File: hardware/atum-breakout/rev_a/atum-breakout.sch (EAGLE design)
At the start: 71 parts, among them J1 TC2030-CTX, J2 TC2030-CC2538-BL, J3 SCREW-TERMINAL_8_0.100, J4 SCREW-TERMINAL_7_0.100, J5 SCREW-TERMINAL_7_0.100, J6 SCREW-TERMINAL_8_0.100, J7 MICRO_USB_B_HIROSE_ZX62R-B-5P, J8 SCREW-TERMINAL_3_0.100, J9 SCREW-TERMINAL_3_0.100, U1 ATUM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

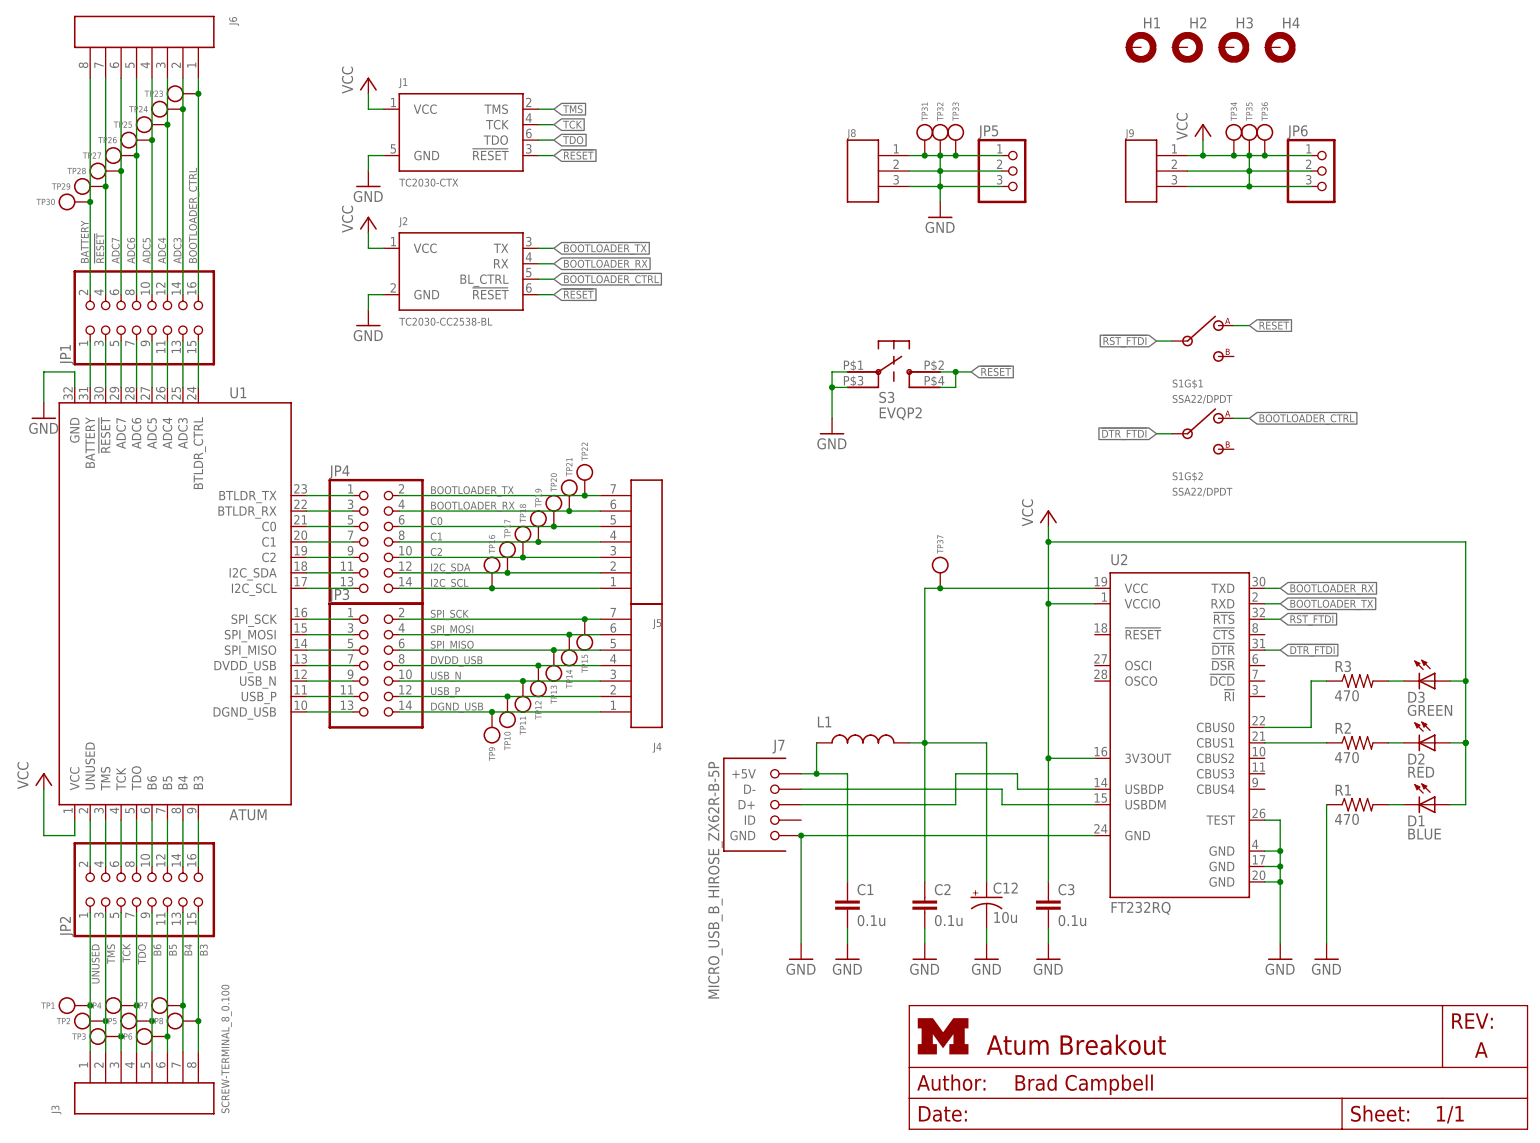
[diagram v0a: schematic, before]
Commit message: updated part labels
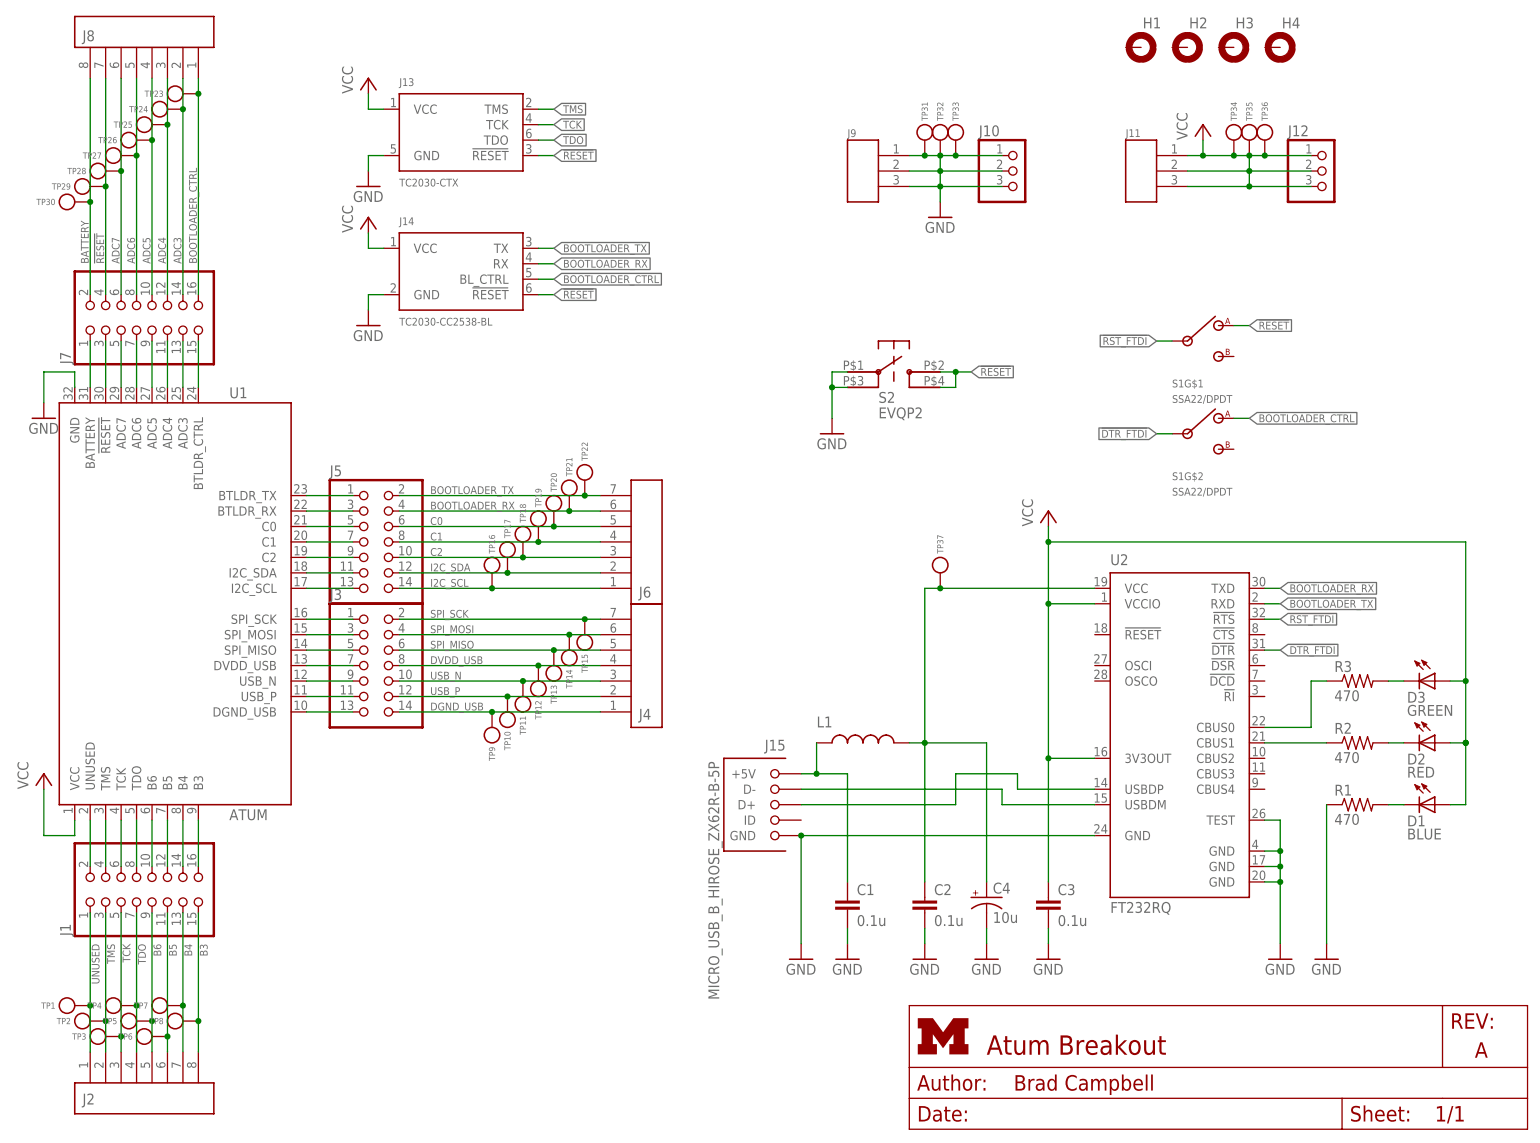
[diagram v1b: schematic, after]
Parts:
- removed JP1, JP2: (no value), pinhead:PINHD-2X8
- removed JP3, JP4: (no value), pinhead:PINHD-2X7
- added J11: SCREW-TERMINAL_3_0.100, headers:SCREW-TERMINAL_3_0.100
- added J13: TC2030-CTX, connector:TC2030-CTX
- added J14: TC2030-CC2538-BL, connector:TC2030-CC2538-BL
- added J15: MICRO_USB_B_HIROSE_ZX62R-B-5P, connector:MICRO_USB_B_HIROSE_ZX62R-B-5P
- J1: value TC2030-CTX -> (none); device connector:TC2030-CTX -> pinhead:PINHD-2X8
- J2: value TC2030-CC2538-BL -> SCREW-TERMINAL_8_0.100; device connector:TC2030-CC2538-BL -> headers:SCREW-TERMINAL_8_0.100
- J3: value SCREW-TERMINAL_8_0.100 -> (none); device headers:SCREW-TERMINAL_8_0.100 -> pinhead:PINHD-2X7
- J5: value SCREW-TERMINAL_7_0.100 -> (none); device headers:SCREW-TERMINAL_7_0.100 -> pinhead:PINHD-2X7
- J6: value SCREW-TERMINAL_8_0.100 -> SCREW-TERMINAL_7_0.100; device headers:SCREW-TERMINAL_8_0.100 -> headers:SCREW-TERMINAL_7_0.100
- J7: value MICRO_USB_B_HIROSE_ZX62R-B-5P -> (none); device connector:MICRO_USB_B_HIROSE_ZX62R-B-5P -> pinhead:PINHD-2X8
- J8: value SCREW-TERMINAL_3_0.100 -> SCREW-TERMINAL_8_0.100; device headers:SCREW-TERMINAL_3_0.100 -> headers:SCREW-TERMINAL_8_0.100
- renumbered C12 to C4, JP5 to J10, JP6 to J12, S3 to S2
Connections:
- net !RESET: now also J13.!RESET, J14.!RESET, J7.3, J7.4, J8.7; no longer J1.!RESET, J2.!RESET, J6.7, JP1.3, JP1.4
- net ADC3: now also J7.13, J7.14, J8.2; no longer J6.2, JP1.13, JP1.14
- net ADC4: now also J7.11, J7.12, J8.3; no longer J6.3, JP1.11, JP1.12
- net ADC5: now also J7.10, J7.9, J8.4; no longer J6.4, JP1.10, JP1.9
- net ADC6: now also J7.7, J7.8, J8.5; no longer J6.5, JP1.7, JP1.8
- net ADC7: now also J7.5, J7.6, J8.6; no longer J6.6, JP1.5, JP1.6
- net B3: now also J1.15, J1.16, J2.8; no longer J3.8, JP2.15, JP2.16
- net B4: now also J1.13, J1.14, J2.7; no longer J3.7, JP2.13, JP2.14
- net B5: now also J1.11, J1.12, J2.6; no longer J3.6, JP2.11, JP2.12
- net B6: now also J1.10, J1.9, J2.5; no longer J3.5, JP2.10, JP2.9
- net BATTERY: now also J7.1, J7.2, J8.8; no longer J6.8, JP1.1, JP1.2
- net BOOTLOADER_CTRL: now also J14.BL_CTRL, J7.15, J7.16, J8.1; no longer J2.BL_CTRL, J6.1, JP1.15, JP1.16
- net BOOTLOADER_RX: now also J14.RX, J5.3, J5.4, J6.6; no longer J2.RX, J5.6, JP4.3, JP4.4
- net BOOTLOADER_TX: now also J14.TX, J5.1, J5.2, J6.7; no longer J2.TX, J5.7, JP4.1, JP4.2
- net C0: now also J5.6, J6.5; no longer JP4.5, JP4.6
- net C1: now also J5.7, J5.8, J6.4; no longer J5.4, JP4.7, JP4.8
- net C2: now also J5.10, J5.9, J6.3; no longer J5.3, JP4.10, JP4.9
- net DGND_USB: now also J3.13, J3.14; no longer JP3.13, JP3.14
- net DVDD_USB: now also J3.7, J3.8; no longer JP3.7, JP3.8
- net GND: now also J13.GND, J14.GND, J15.GND, J9.1, J9.2, J9.3; no longer J1.GND, J2.GND, J7.GND, J8.1, J8.2, J8.3
- net I2C_SCL: now also J5.13, J5.14, J6.1; no longer J5.1, JP4.13, JP4.14
- net I2C_SDA: now also J5.11, J5.12, J6.2; no longer J5.2, JP4.11, JP4.12
- net N$3: now also J15.D-; no longer J7.D-
- net N$4: now also J15.D+; no longer J7.D+
- net SPI_MISO: now also J3.5, J3.6; no longer JP3.5, JP3.6
- net SPI_MOSI: now also J3.3, J3.4; no longer JP3.3, JP3.4
- net SPI_SCK: now also J3.1, J3.2; no longer JP3.1, JP3.2
- net TCK: now also J1.5, J1.6, J13.TCK, J2.3; no longer J1.TCK, J3.3, JP2.5, JP2.6
- net TDO: now also J1.7, J1.8, J13.TDO, J2.4; no longer J1.TDO, J3.4, JP2.7, JP2.8
- net TMS: now also J1.3, J1.4, J13.TMS, J2.2; no longer J1.TMS, J3.2, JP2.3, JP2.4
- net UNUSED: now also J1.1, J1.2, J2.1; no longer J3.1, JP2.1, JP2.2
- net USB5V: now also J15.+5V; no longer J7.+5V
- net USB_N: now also J3.10, J3.9; no longer JP3.10, JP3.9
- net USB_P: now also J3.11, J3.12; no longer JP3.11, JP3.12
- net VCC: now also J11.1, J11.2, J11.3, J13.VCC, J14.VCC; no longer J1.VCC, J2.VCC, J9.1, J9.2, J9.3
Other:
- moved on the sheet: J9

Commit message: atum breakout bom
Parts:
- J1, J7: DIGIKEY (none) -> 609-3364-ND; MOUSER (none) -> 649-68602-116HLF; NEWARK (none) -> 20M2833
- J15: MOUSER (none) -> 798-ZX62R-B-5P; NEWARK (none) -> 69W0714
- J3, J5: DIGIKEY (none) -> 609-3491-ND; MOUSER (none) -> 649-67996-114HLF; NEWARK (none) -> 30M1973
- S1: DIGIKEY (none) -> 450-1604-ND; MOUSER (none) -> 506-SSA22; NEWARK (none) -> 50F5561
- S2: MOUSER (none) -> 667-EVQ-P2K02Q
- U2: DIGIKEY (none) -> 768-1008-1-ND
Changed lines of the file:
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@@
 <part name="GND2" library="supply1" deviceset="GND" device=""/>
 <part name="P+2" library="supply1" deviceset="VCC" device=""/>
-<part name="J7" library="pinhead" deviceset="PINHD-2X8" device=""/>
-<part name="J1" library="pinhead" deviceset="PINHD-2X8" device=""/>
-<part name="J3" library="pinhead" deviceset="PINHD-2X7" device=""/>
-<part name="J5" library="pinhead" deviceset="PINHD-2X7" device=""/>
+<part name="J7" library="pinhead" deviceset="PINHD-2X8" device="">
+<attribute name="DIGIKEY" value="609-3364-ND"/>
+<attribute name="MOUSER" value="649-68602-116HLF"/>
+<attribute name="NEWARK" value="20M2833"/>
+</part>
+<part name="J1" library="pinhead" deviceset="PINHD-2X8" device="">
+<attribute name="DIGIKEY" value="609-3364-ND"/>
+<attribute name="MOUSER" value="649-68602-116HLF"/>
+<attribute name="NEWARK" value="20M2833"/>
+</part>
+<part name="J3" library="pinhead" deviceset="PINHD-2X7" device="">
+<attribute name="DIGIKEY" value="609-3491-ND"/>
+<attribute name="MOUSER" value="649-67996-114HLF"/>
+<attribute name="NEWARK" value="30M1973"/>
+</part>
+<part name="J5" library="pinhead" deviceset="PINHD-2X7" device="">
+<attribute name="DIGIKEY" value="609-3491-ND"/>
+<attribute name="MOUSER" value="649-67996-114HLF"/>
+<attribute name="NEWARK" value="30M1973"/>
+</part>
 <part name="J2" library="headers" deviceset="SCREW-TERMINAL_8_0.100" device=""/>
 <part name="TP1" library="headers" deviceset="TEST_POINT_0.040IN" device=""/>
@@
 <part name="D2" library="SparkFun" deviceset="LED" device="0603" value="RED"/>
 <part name="D3" library="SparkFun" deviceset="LED" device="0603" value="GREEN"/>
-<part name="J15" library="connector" deviceset="MICRO_USB_B_HIROSE_ZX62R-B-5P" device=""/>
+<part name="J15" library="connector" deviceset="MICRO_USB_B_HIROSE_ZX62R-B-5P" device="">
+<attribute name="MOUSER" value="798-ZX62R-B-5P"/>
+<attribute name="NEWARK" value="69W0714"/>
+</part>
 <part name="D1" library="SparkFun" deviceset="LED" device="0603" value="BLUE"/>
 <part name="R1" library="rcl" deviceset="R-US_" device="R0603" value="470"/>
 <part name="GND9" library="supply1" deviceset="GND" device=""/>
-<part name="U2" library="ftdichip" deviceset="FT232R" device="Q"/>
+<part name="U2" library="ftdichip" deviceset="FT232R" device="Q">
+<attribute name="DIGIKEY" value="768-1008-1-ND"/>
+</part>
 <part name="P+3" library="supply1" deviceset="VCC" device=""/>
-<part name="S1" library="switches" deviceset="SSA22/DPDT" device=""/>
+<part name="S1" library="switches" deviceset="SSA22/DPDT" device="">
+<attribute name="DIGIKEY" value="450-1604-ND"/>
+<attribute name="MOUSER" value="506-SSA22"/>
+<attribute name="NEWARK" value="50F5561"/>
+</part>
 <part name="S2" library="berkeley-epic" deviceset="EVQP2" device="">
 <attribute name="DIGIKEY" value="P11084SCT-ND"/>
+<attribute name="MOUSER" value="667-EVQ-P2K02Q"/>
 </part>
 <part name="GND10" library="supply1" deviceset="GND" device=""/>
@@
 <attribute name="NAME" x="9.525" y="125.73" size="1.778" layer="95" rot="R90"/>
 <attribute name="VALUE" x="35.56" y="125.73" size="1.778" layer="96" rot="R90"/>
+<attribute name="DIGIKEY" x="20.32" y="132.08" size="1.778" layer="96" rot="R90" display="off"/>
+<attribute name="MOUSER" x="20.32" y="132.08" size="1.778" layer="96" rot="R90" display="off"/>
+<attribute name="NEWARK" x="20.32" y="132.08" size="1.778" layer="96" rot="R90" display="off"/>
 </instance>
 <instance part="J1" gate="A" x="20.32" y="38.1" smashed="yes" rot="R90">
 <attribute name="NAME" x="9.525" y="31.75" size="1.778" layer="95" rot="R90"/>
 <attribute name="VALUE" x="35.56" y="31.75" size="1.778" layer="96" rot="R90"/>
+<attribute name="MOUSER" x="20.32" y="38.1" size="1.778" layer="96" rot="R90" display="off"/>
+<attribute name="DIGIKEY" x="20.32" y="38.1" size="1.778" layer="96" rot="R90" display="off"/>
+<attribute name="NEWARK" x="20.32" y="38.1" size="1.778" layer="96" rot="R90" display="off"/>
 </instance>
 <instance part="J3" gate="A" x="58.42" y="76.2" smashed="yes">
 <attribute name="NAME" x="52.07" y="86.995" size="1.778" layer="95"/>
 <attribute name="VALUE" x="52.07" y="63.5" size="1.778" layer="96"/>
+<attribute name="DIGIKEY" x="58.42" y="76.2" size="1.778" layer="96" display="off"/>
+<attribute name="MOUSER" x="58.42" y="76.2" size="1.778" layer="96" display="off"/>
+<attribute name="NEWARK" x="58.42" y="76.2" size="1.778" layer="96" display="off"/>
 </instance>
 <instance part="J5" gate="A" x="58.42" y="96.52" smashed="yes">
 <attribute name="NAME" x="52.07" y="107.315" size="1.778" layer="95"/>
 <attribute name="VALUE" x="52.07" y="83.82" size="1.778" layer="96"/>
+<attribute name="DIGIKEY" x="58.42" y="96.52" size="1.778" layer="96" display="off"/>
+<attribute name="MOUSER" x="58.42" y="96.52" size="1.778" layer="96" display="off"/>
+<attribute name="NEWARK" x="58.42" y="96.52" size="1.778" layer="96" display="off"/>
 </instance>
 <instance part="J2" gate="G$1" x="20.32" y="5.08" smashed="yes" rot="R90">
@@
 <attribute name="NAME" x="127" y="62.23" size="1.778" layer="95" rot="MR0"/>
 <attribute name="VALUE" x="116.078" y="60.452" size="1.778" layer="95" rot="MR270"/>
+<attribute name="MOUSER" x="121.92" y="53.34" size="1.778" layer="96" rot="MR0" display="off"/>
+<attribute name="NEWARK" x="121.92" y="53.34" size="1.778" layer="96" rot="MR0" display="off"/>
 </instance>
 <instance part="D1" gate="G$1" x="233.68" y="53.34" rot="R270"/>
 <instance part="R1" gate="G$1" x="220.98" y="53.34"/>
 <instance part="GND9" gate="1" x="215.9" y="27.94"/>
-<instance part="U2" gate="1" x="190.5" y="66.04"/>
+<instance part="U2" gate="1" x="190.5" y="66.04">
+<attribute name="DIGIKEY" x="190.5" y="66.04" size="1.778" layer="96" display="off"/>
+</instance>
 <instance part="P+3" gate="VCC" x="170.18" y="101.6"/>
-<instance part="S1" gate="G$1" x="193.04" y="129.54"/>
+<instance part="S1" gate="G$1" x="193.04" y="129.54">
+<attribute name="DIGIKEY" x="193.04" y="129.54" size="1.778" layer="96" display="off"/>
+<attribute name="MOUSER" x="193.04" y="129.54" size="1.778" layer="96" display="off"/>
+<attribute name="NEWARK" x="193.04" y="129.54" size="1.778" layer="96" display="off"/>
+</instance>
 <instance part="S1" gate="G$2" x="193.04" y="114.3"/>
 <instance part="S2" gate="G$1" x="144.78" y="121.92">
 <attribute name="DIGIKEY" x="144.78" y="121.92" size="1.27" layer="96" display="off"/>
+<attribute name="MOUSER" x="144.78" y="121.92" size="1.778" layer="96" display="off"/>
 </instance>
 <instance part="GND10" gate="1" x="134.62" y="114.3"/>
